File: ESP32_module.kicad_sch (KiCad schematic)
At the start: 25 parts, among them J3 GSD090012SEU, U2 CP2102N-Axx-xQFN20, U3 USBLC6-2SC6, U4 W25Q32JVSSIQ, U5 ESP32-C3-WROOM-02-H4

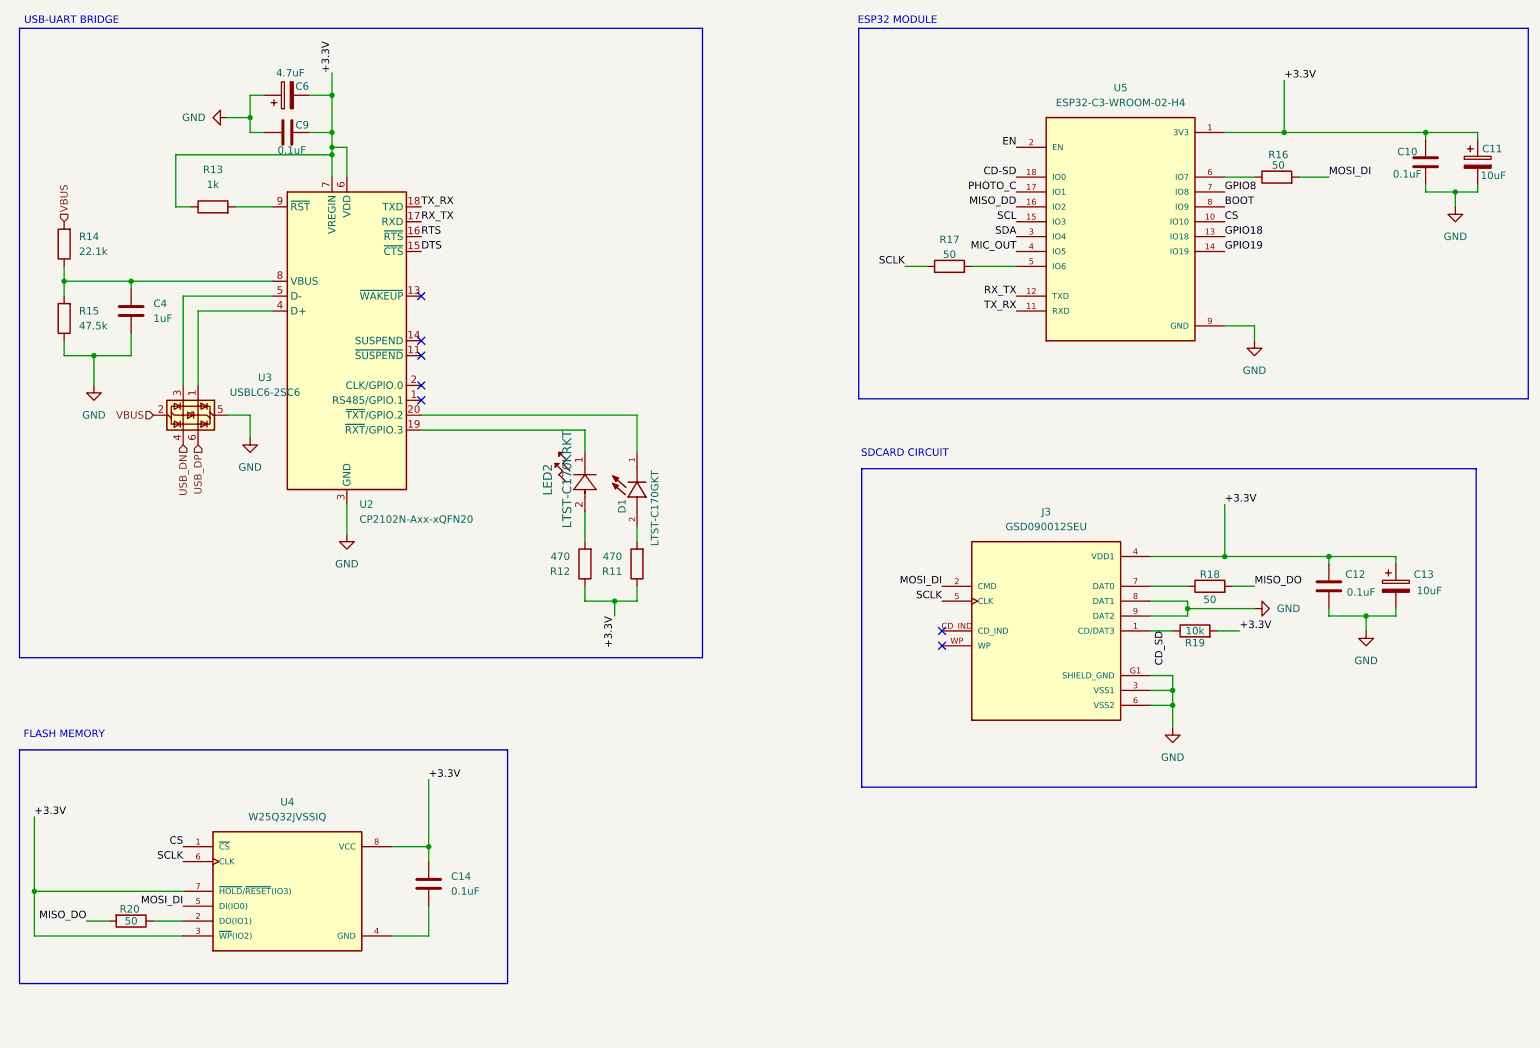
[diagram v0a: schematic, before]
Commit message: Completed Sheet 3- Sensors and Sheet 4- User Interface
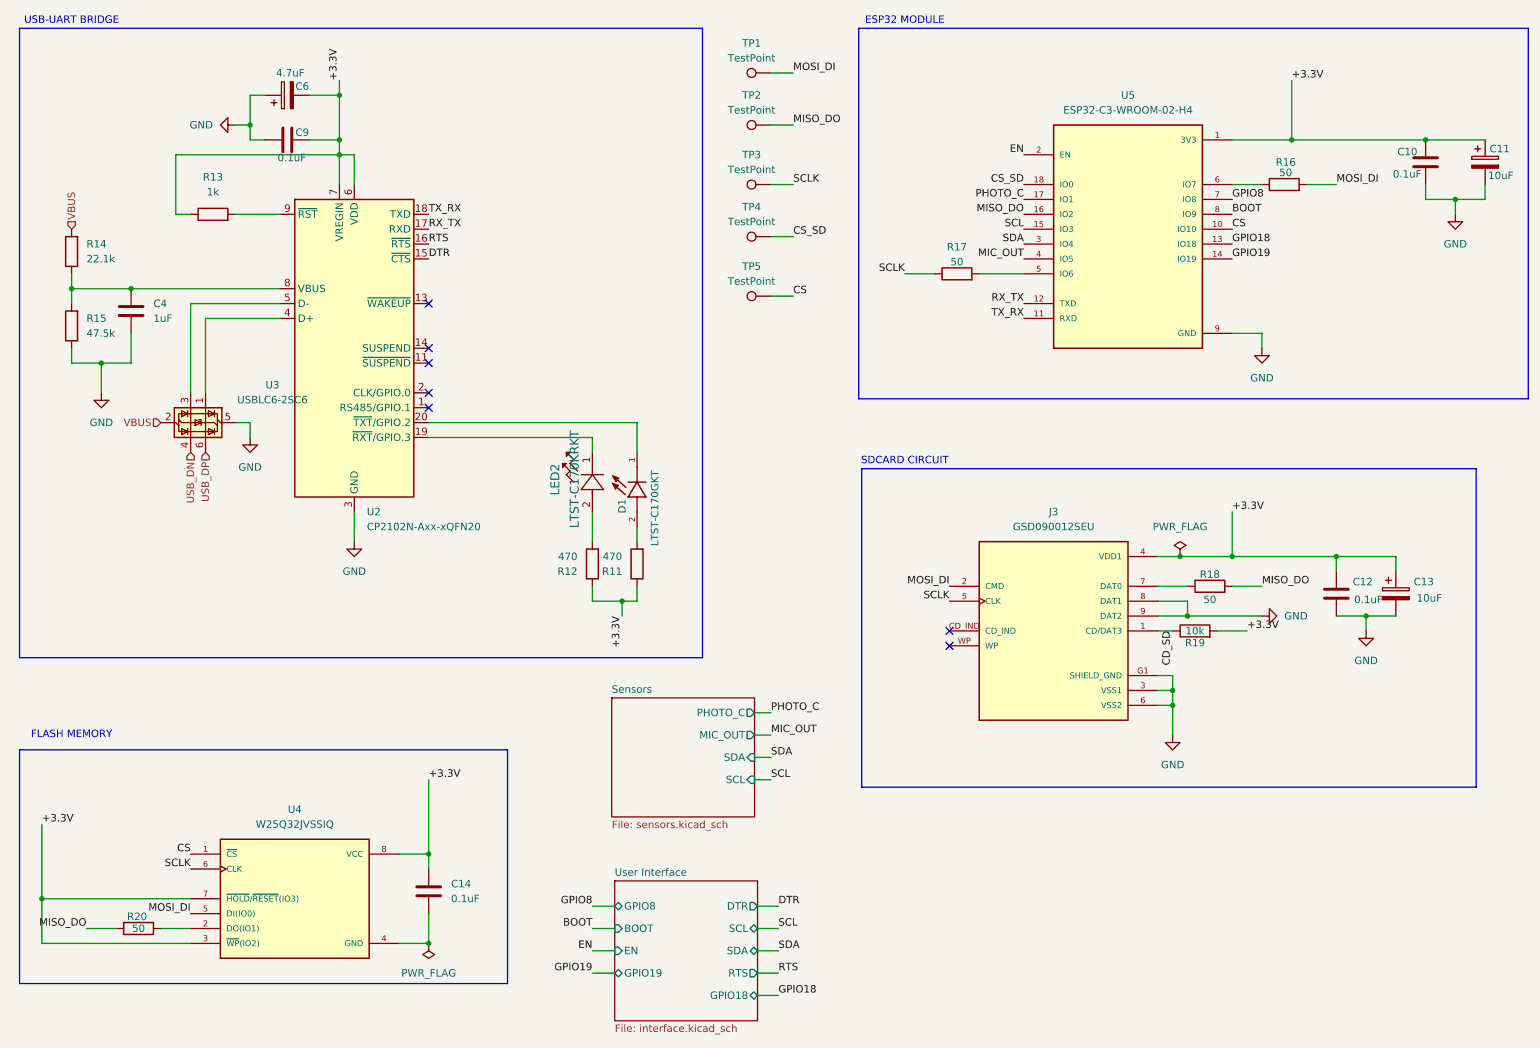
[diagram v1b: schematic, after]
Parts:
- added TP1, TP2, TP3, TP4, TP5: TestPoint, symbol Connector:TestPoint
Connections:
- net MISO_DD is gone; now on net MISO_DO: U5.16 (IO2)
- net CS: now also TP5.1
- net MISO_DO: now also TP2.1
- net MOSI_DI: now also TP1.1
- net SCLK: now also TP3.1
- net CD-SD renamed CS_SD
- net CS_SD: now also TP4.1
- net DTS renamed DTR
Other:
- added sheet Sensors (sensors.kicad_sch)
- added sheet User Interface (interface.kicad_sch)
- moved on the sheet: C11, C12, C13, C14, C9, J3, LED2, R12, R13, R14, R15, R16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

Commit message: Completed Schematic Layout
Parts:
- C10, C11, C12, C13, C14, C6, C9, R11, R12, R13, R14, R15, R16, R17, R18, R19, R20: footprint (none) -> Resistor_SMD:R_0805_2012Metric
- C4: footprint (none) -> Capacitor_SMD:C_0805_2012Metric
- D1: footprint LTST-C170GKT:LED_LTST-C170GKT -> Resistor_SMD:R_0805_2012Metric
- J3: footprint GSD090012SEU:AMPHENOL_GSD090012SEU -> Resistor_SMD:R_0805_2012Metric
- LED2: footprint LED_LTST-C170KRKT_LTO -> Resistor_SMD:R_0805_2012Metric
- TP1, TP2, TP3, TP4, TP5: footprint (none) -> TestPoint:TestPoint_Pad_D1.0mm
- U2: footprint Package_DFN_QFN:SiliconLabs_QFN-20-1EP_3x3mm_P0.5mm -> Package_DFN_QFN:SiliconLabs_QFN-20-1EP_3x3mm_P0.5mm_EP1.8x1.8mm
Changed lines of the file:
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@@
 			)
 		)
-		(property "Footprint" ""
+		(property "Footprint" "Resistor_SMD:R_0805_2012Metric"
 			(at 41.91 178.562 90)
 			(effects
@@
 			)
 		)
-		(property "Footprint" ""
+		(property "Footprint" "TestPoint:TestPoint_Pad_D1.0mm"
 			(at 149.86 48.26 0)
 			(effects
@@
 			)
 		)
-		(property "Footprint" "LED_LTST-C170KRKT_LTO"
+		(property "Footprint" "Resistor_SMD:R_0805_2012Metric"
 			(at 119.38 109.22 0)
 			(effects
@@
 			)
 		)
-		(property "Footprint" ""
+		(property "Footprint" "Resistor_SMD:R_0805_2012Metric"
 			(at 121.158 118.11 90)
 			(effects
@@
 			)
 		)
-		(property "Footprint" ""
+		(property "Footprint" "Resistor_SMD:R_0805_2012Metric"
 			(at 92.4052 177.8 0)
 			(effects
@@
 			)
 		)
-		(property "Footprint" ""
+		(property "Footprint" "Resistor_SMD:R_0805_2012Metric"
 			(at 181.61 70.358 90)
 			(effects
@@
 			)
 		)
-		(property "Footprint" ""
+		(property "Footprint" "TestPoint:TestPoint_Pad_D1.0mm"
 			(at 149.86 38.1 0)
 			(effects
@@
 			)
 		)
-		(property "Footprint" ""
+		(property "Footprint" "TestPoint:TestPoint_Pad_D1.0mm"
 			(at 149.86 67.31 0)
 			(effects
@@
 			)
 		)
-		(property "Footprint" ""
+		(property "Footprint" "Resistor_SMD:R_0805_2012Metric"
 			(at 224.79 123.698 90)
 			(effects
@@
 			)
 		)
-		(property "Footprint" ""
+		(property "Footprint" "Resistor_SMD:R_0805_2012Metric"
 			(at 32.258 64.77 90)
 			(effects
@@
 			)
 		)
-		(property "Footprint" ""
+		(property "Footprint" "Resistor_SMD:R_0805_2012Metric"
 			(at 247.3452 127 0)
 			(effects
@@
 			)
 		)
-		(property "Footprint" ""
+		(property "Footprint" "Resistor_SMD:R_0805_2012Metric"
 			(at 71.12 37.1348 0)
 			(effects
@@
 			)
 		)
-		(property "Footprint" ""
+		(property "Footprint" "Resistor_SMD:R_0805_2012Metric"
 			(at 257.5052 127 0)
 			(effects
@@
 			)
 		)
-		(property "Footprint" "LTST-C170GKT:LED_LTST-C170GKT"
+		(property "Footprint" "Resistor_SMD:R_0805_2012Metric"
 			(at 127 104.14 0)
 			(effects
@@
 			)
 		)
-		(property "Footprint" ""
+		(property "Footprint" "Resistor_SMD:R_0805_2012Metric"
 			(at 54.61 60.198 90)
 			(effects
@@
 			)
 		)
-		(property "Footprint" "GSD090012SEU:AMPHENOL_GSD090012SEU"
+		(property "Footprint" "Resistor_SMD:R_0805_2012Metric"
 			(at 198.12 129.54 0)
 			(effects
@@
 			)
 		)
-		(property "Footprint" ""
+		(property "Footprint" "Resistor_SMD:R_0805_2012Metric"
 			(at 128.778 118.11 90)
 			(effects
@@
 			)
 		)
-		(property "Footprint" ""
+		(property "Footprint" "Resistor_SMD:R_0805_2012Metric"
 			(at 260.6548 45.72 0)
 			(effects
@@
 			)
 		)
-		(property "Footprint" ""
+		(property "Footprint" "Resistor_SMD:R_0805_2012Metric"
 			(at 32.258 77.47 90)
 			(effects
@@
 			)
 		)
-		(property "Footprint" ""
+		(property "Footprint" "Resistor_SMD:R_0805_2012Metric"
 			(at 237.49 55.118 90)
 			(effects
@@
 			)
 		)
-		(property "Footprint" ""
+		(property "Footprint" "Capacitor_SMD:C_0805_2012Metric"
 			(at 41.6052 78.74 0)
 			(effects
@@
 			)
 		)
-		(property "Footprint" ""
+		(property "Footprint" "Resistor_SMD:R_0805_2012Metric"
 			(at 272.7452 53.34 0)
 			(effects
@@
 			)
 		)
-		(property "Footprint" "Package_DFN_QFN:SiliconLabs_QFN-20-1EP_3x3mm_P0.5mm"
+		(property "Footprint" "Package_DFN_QFN:SiliconLabs_QFN-20-1EP_3x3mm_P0.5mm_EP1.8x1.8mm"
 			(at 110.49 107.95 0)
 			(effects
@@
 			)
 		)
-		(property "Footprint" ""
+		(property "Footprint" "TestPoint:TestPoint_Pad_D1.0mm"
 			(at 149.86 57.15 0)
 			(effects
@@
 			)
 		)
-		(property "Footprint" ""
+		(property "Footprint" "Resistor_SMD:R_0805_2012Metric"
 			(at 222.25 131.318 90)
 			(effects
@@
 			)
 		)
-		(property "Footprint" ""
+		(property "Footprint" "TestPoint:TestPoint_Pad_D1.0mm"
 			(at 149.86 29.21 0)
 			(effects
@@
 			)
 		)
-		(property "Footprint" ""
+		(property "Footprint" "Resistor_SMD:R_0805_2012Metric"
 			(at 71.12 44.7548 0)
 			(effects
